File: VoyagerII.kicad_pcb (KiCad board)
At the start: 2 copper layers, 285 x 95.1 mm, 262 parts, among them P1 TC2030-IDC, SW1 SW_PUSH, U1 ATXMEGA32A4U-AU, U2 MCP1700T-3002E/TT, U3 PRTR5V0U2X, U4 IS31FL3731-SALS2, U5 74LVC1G34

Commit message: Adjust line weight for deco
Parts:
- added G***: LOGO, locallib:icon-7.6, F.Cu at (215.5, 133.3)
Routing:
- net COL6: track 144.3 -> 141.3 mm
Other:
- board text added: "CLK"
- board text added: "VCC"
- board text removed: "3.3V"
- board text removed: "PDICLK"

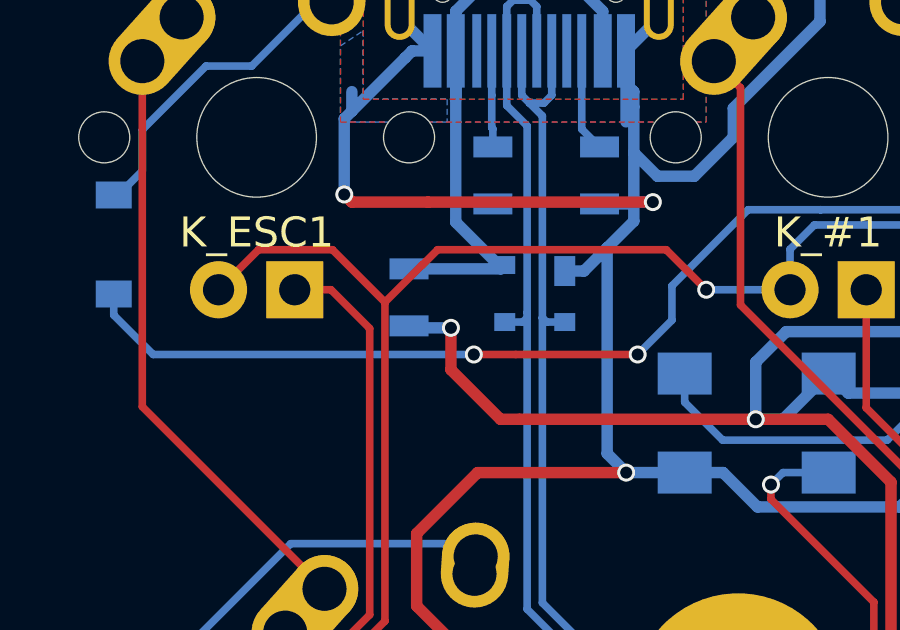
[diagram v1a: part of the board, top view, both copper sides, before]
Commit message: Tune component labels
Horizontal for system, vertical for matrix
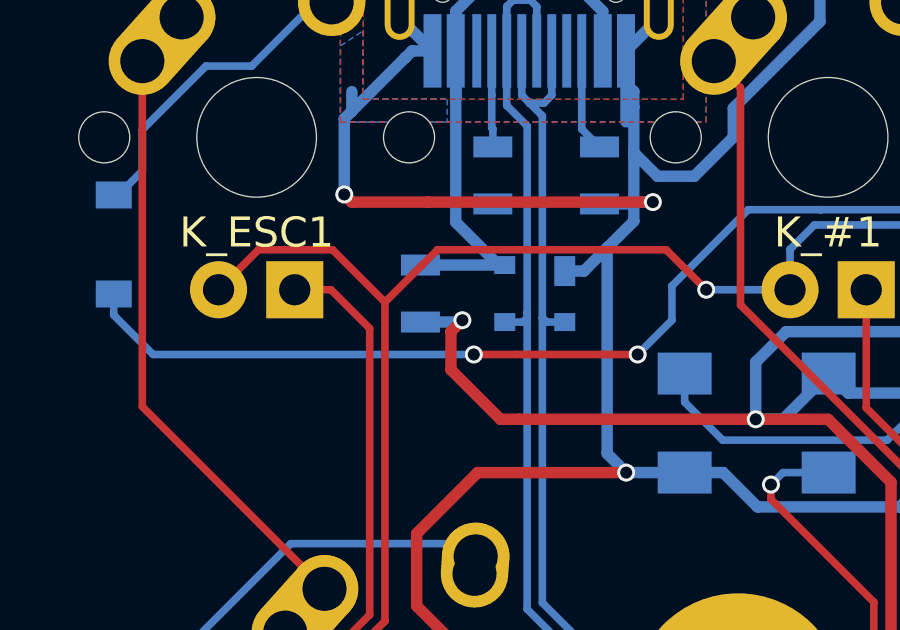
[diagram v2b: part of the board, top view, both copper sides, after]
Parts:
- moved F1 0.40 mm to (62.6, 62.4)
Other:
- board text removed: "Rev. 1.0"
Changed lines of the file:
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@@
     (area 28.932287 28.25625 334.504151 153.909376)
     (thickness 1.6)
-    (drawings 47)
+    (drawings 49)
     (tracks 3211)
     (zones 0)
@@
     (tags "capacitor 0805")
     (attr smd)
-    (fp_text reference C2 (at 0 1.651 270) (layer B.SilkS)
+    (fp_text reference C2 (at -2.54 0 360) (layer B.SilkS)
       (effects (font (size 1 1) (thickness 0.15)) (justify mirror))
     )
@@
     (tags "capacitor 0805")
     (attr smd)
-    (fp_text reference C4 (at 0 1.778 90) (layer B.SilkS)
+    (fp_text reference C4 (at 0 2.032 180) (layer B.SilkS)
       (effects (font (size 1 1) (thickness 0.15)) (justify mirror))
     )
@@
     (tags "resistor 0805")
     (attr smd)
-    (fp_text reference R1 (at 0 -1.778 450) (layer B.SilkS)
+    (fp_text reference R1 (at 0 -2.032 540) (layer B.SilkS)
       (effects (font (size 1 1) (thickness 0.15)) (justify mirror))
     )
@@
     (tags SOD-123)
     (attr smd)
-    (fp_text reference D15 (at 0 2) (layer B.SilkS)
+    (fp_text reference D15 (at -3.175 -0.015875 90) (layer B.SilkS)
       (effects (font (size 1 1) (thickness 0.15)) (justify mirror))
     )
@@
     (tags SOD-123)
     (attr smd)
-    (fp_text reference D29 (at 0 2) (layer B.SilkS)
+    (fp_text reference D29 (at -3.190875 0.015875 90) (layer B.SilkS)
       (effects (font (size 1 1) (thickness 0.15)) (justify mirror))
     )
@@
     (clearance 0.127)
     (attr virtual)
-    (fp_text reference P1 (at -3.048 -2.54 540) (layer B.SilkS)
+    (fp_text reference P1 (at -3.048 2.54 540) (layer B.SilkS)
       (effects (font (size 0.75692 0.75692) (thickness 0.127)) (justify mirror))
     )
@@
     (tags "resistor 0805")
     (attr smd)
-    (fp_text reference R2 (at 0 1.65 270) (layer B.SilkS)
+    (fp_text reference R2 (at 0 2.032 360) (layer B.SilkS)
       (effects (font (size 1 1) (thickness 0.15)) (justify mirror))
     )
@@
     (tags "resistor 0805")
     (attr smd)
-    (fp_text reference R3 (at 0 1.65 90) (layer B.SilkS)
+    (fp_text reference R3 (at -2.413 0 180) (layer B.SilkS)
       (effects (font (size 1 1) (thickness 0.15)) (justify mirror))
     )
@@
     (tags "resistor 0805")
     (attr smd)
-    (fp_text reference R4 (at 0 1.65 90) (layer B.SilkS)
+    (fp_text reference R4 (at -2.413 0 180) (layer B.SilkS)
       (effects (font (size 1 1) (thickness 0.15)) (justify mirror))
     )
@@
     (tags "capacitor 0805")
     (attr smd)
-    (fp_text reference CRGB1 (at 2.54 -1.778 360) (layer B.SilkS)
+    (fp_text reference CRGB1 (at 2.54 -2.032 360) (layer B.SilkS)
       (effects (font (size 1 1) (thickness 0.15)) (justify mirror))
     )
@@
     (tags "resistor 0805")
     (attr smd)
-    (fp_text reference R5 (at 0 1.65 90) (layer B.SilkS)
+    (fp_text reference R5 (at 0 -2.032 180) (layer B.SilkS)
       (effects (font (size 1 1) (thickness 0.15)) (justify mirror))
     )
@@
     (tags "SOT-353 SC-70-5")
     (attr smd)
-    (fp_text reference U5 (at -0.762 -2.159) (layer B.SilkS)
+    (fp_text reference U5 (at -2.54 0) (layer B.SilkS)
       (effects (font (size 1 1) (thickness 0.15)) (justify mirror))
     )
@@
   )
   (module Resistors_SMD:R_0805 (layer B.Cu)
-    (at 62.23 62.484 90)
+    (at 62.611 62.357 90)
     (descr "Resistor SMD 0805, reflow soldering, Vishay (see dcrcw.pdf)")
     (tags "resistor 0805")
     (attr smd)
-    (fp_text reference F1 (at 2.286 -0.0635 180) (layer B.SilkS)
+    (fp_text reference F1 (at -2.413 0 180) (layer B.SilkS)
       (effects (font (size 1 1) (thickness 0.15)) (justify mirror))
     )
@@
   (module locallib:SOT143B (layer B.Cu)
     (at 66.421 62.357 270)
-    (fp_text reference U3 (at -2.286 -0.0635 540) (layer B.SilkS)
+    (fp_text reference U3 (at 2.413 0 540) (layer B.SilkS)
       (effects (font (size 1 1) (thickness 0.15)) (justify mirror))
     )
@@
     (tags SOD-123)
     (attr smd)
-    (fp_text reference D63 (at 0 2 90) (layer B.SilkS)
+    (fp_text reference D63 (at 0.53975 -1.93675 90) (layer B.SilkS)
       (effects (font (size 1 1) (thickness 0.15)) (justify mirror))
     )
@@
     (tags SOD-123)
     (attr smd)
-    (fp_text reference D64 (at 0 2) (layer B.SilkS)
+    (fp_text reference D64 (at -3.20675 -0.015875 90) (layer B.SilkS)
       (effects (font (size 1 1) (thickness 0.15)) (justify mirror))
     )
@@
     (tags "resistor 0805")
     (attr smd)
-    (fp_text reference R6 (at 0.762 1.778 270) (layer B.SilkS)
+    (fp_text reference R6 (at -1.016 -2.032 360) (layer B.SilkS)
       (effects (font (size 1 1) (thickness 0.15)) (justify mirror))
     )
@@
     (tags "resistor 0805")
     (attr smd)
-    (fp_text reference R7 (at 2.413 -0.254 360) (layer B.SilkS)
+    (fp_text reference R7 (at 1.016 -2.032 360) (layer B.SilkS)
       (effects (font (size 1 1) (thickness 0.15)) (justify mirror))
     )
@@
       (xy 1.69672 0.335006) (xy 1.69672 1.69672)) (layer F.Mask) (width 0.01))
   )
+  (gr_line (start 70.739 55.88) (end 70.739 53.467) (layer B.SilkS) (width 0.3))
+  (gr_line (start 61.722 55.88) (end 70.739 55.88) (layer B.SilkS) (width 0.3))
+  (gr_line (start 61.722 53.467) (end 61.722 55.88) (layer B.SilkS) (width 0.3))
   (gr_text "Rev 1.5" (at 66.167 50.419) (layer B.SilkS)
     (effects (font (size 1 1) (thickness 0.15)) (justify mirror))
@@
     (arrow2b (pts (xy 36.068 47.879) (xy 35.481579 46.752496)))
   )
-  (gr_text "Rev. 1.0" (at 145.669 140.335) (layer B.SilkS)
-    (effects (font (size 1 1) (thickness 0.15)) (justify mirror))
-  )
   (gr_line (start 210.058 130.937) (end 210.058 136.017) (layer B.SilkS) (width 0.15))
   (gr_text "Lo and\nBehold!" (at 207.899 133.477 90) (layer B.SilkS)
@@
   (segment (start 136.255 134.618) (end 135.310499 135.562501) (width 0.381) (layer B.Cu) (net 2) (status 10))
   (segment (start 135.310499 135.562501) (end 130.500501 135.562501) (width 0.381) (layer B.Cu) (net 2))
+  (segment (start 64.008 63.246) (end 63.627 63.627) (width 0.381) (layer F.Cu) (net 3))
+  (segment (start 63.627 63.627) (end 63.627 64.897) (width 0.381) (layer F.Cu) (net 3))
+  (segment (start 62.611 63.307) (end 63.947 63.307) (width 0.381) (layer B.Cu) (net 3))
+  (segment (start 63.947 63.307) (end 64.008 63.246) (width 0.381) (layer B.Cu) (net 3))
+  (via (at 64.008 63.246) (size 0.6) (drill 0.4) (layers F.Cu B.Cu) (net 3))
   (segment (start 155.448 65.659) (end 155.448 108.712) (width 0.381) (layer F.Cu) (net 3))
   (segment (start 155.448 108.712) (end 156.337 109.601) (width 0.381) (layer F.Cu) (net 3))
@@
   (segment (start 236.461138 128.003138) (end 236.347 127.889) (width 0.381) (layer B.Cu) (net 3))
   (via (at 236.347 127.889) (size 0.6) (drill 0.4) (layers F.Cu B.Cu) (net 3))
-  (segment (start 63.627 63.5) (end 62.296 63.5) (width 0.381) (layer B.Cu) (net 3))
-  (segment (start 62.296 63.5) (end 62.23 63.434) (width 0.381) (layer B.Cu) (net 3))
   (segment (start 65.278 66.548) (end 63.627 64.897) (width 0.381) (layer F.Cu) (net 3))
-  (segment (start 63.627 64.897) (end 63.627 63.5) (width 0.381) (layer F.Cu) (net 3))
-  (via (at 63.627 63.5) (size 0.6) (drill 0.4) (layers F.Cu B.Cu) (net 3))
   (segment (start 65.913 66.548) (end 65.278 66.548) (width 0.381) (layer F.Cu) (net 3))
   (segment (start 73.787 66.548) (end 76.2 66.548) (width 0.381) (layer F.Cu) (net 3))
@@
   (via (at 132.715 129.413) (size 0.6) (drill 0.4) (layers F.Cu B.Cu) (net 3))
   (via (at 153.83404 137.460048) (size 0.6) (drill 0.4) (layers F.Cu B.Cu) (net 3))
+  (segment (start 62.611 61.407) (end 65.421 61.407) (width 0.381) (layer B.Cu) (net 4))
   (segment (start 65.217 61.407) (end 65.421 61.407) (width 0.381) (layer B.Cu) (net 4))
   (segment (start 63.7876 59.9776) (end 65.217 61.407) (width 0.381) (layer B.Cu) (net 4))
@@
   (segment (start 67.746412 52.00649) (end 68.6876 52.947678) (width 0.381) (layer B.Cu) (net 4))
   (segment (start 68.6876 52.947678) (end 68.6876 54.269) (width 0.381) (layer B.Cu) (net 4))
-  (segment (start 62.23 61.534) (end 65.294 61.534) (width 0.381) (layer B.Cu) (net 4))
-  (segment (start 65.294 61.534) (end 65.421 61.407) (width 0.381) (layer B.Cu) (net 4))
   (segment (start 155.067 129.032) (end 154.813 128.778) (width 0.254) (layer F.Cu) (net 5))
   (segment (start 164.592 138.049) (end 163.957 137.414) (width 0.254) (layer F.Cu) (net 5) (status 10))

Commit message: Update readme
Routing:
- net GND: track 1577.1 -> 1592.0 mm, vias 72 -> 74
- net LED-A4: track 224.5 -> 223.7 mm

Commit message: Add logo
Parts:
- added G***: LOGO, locallib:ai-7.6, F.Cu at (227.4, 133.3)
- added REF**: ai03-20mil, locallib:ai03-20mil, B.Cu at (73.8, 133.2)
- moved G*** 0.65 mm to (216.2, 133.3)

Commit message: Finalize PCB, DRC checks
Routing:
- net GND: track 1592.0 -> 1590.9 mm
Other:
- net class Default: clearance 0.2032 -> 0.1778
- net class Power: clearance 0.2032 -> 0.1778
- rule trace_clearance: 0.2032 -> 0.1778
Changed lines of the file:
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@@
 (kicad_pcb (version 4) (host pcbnew 4.0.7)
   (general
-    (links 0)
-    (no_connects 1)
+    (links 646)
+    (no_connects 0)
     (area 28.932287 28.25625 334.504151 153.909376)
     (thickness 1.6)
     (drawings 43)
-    (tracks 3236)
+    (tracks 3224)
     (zones 0)
     (modules 265)
@@
   (setup
     (last_trace_width 0.254)
-    (trace_clearance 0.2032)
+    (trace_clearance 0.1778)
     (zone_clearance 0.381)
     (zone_45_only no)
@@
   (net 143 "Net-(USB1-Pad3)")
   (net_class Default "This is the default net class."
-    (clearance 0.2032)
+    (clearance 0.1778)
     (trace_width 0.254)
     (via_dia 0.6)
@@
   )
   (net_class Power ""
-    (clearance 0.2032)
+    (clearance 0.1778)
     (trace_width 0.381)
     (via_dia 0.6)
@@
   (segment (start 153.807 132.318) (end 153.188 131.699) (width 0.381) (layer B.Cu) (net 1))
   (segment (start 153.188 131.699) (end 151.1785 131.699) (width 0.381) (layer B.Cu) (net 1) (status 20))
-  (segment (start 66.167 48.674) (end 61.9176 48.674) (width 0.381) (layer B.Cu) (net 2))
-  (segment (start 70.5576 48.674) (end 66.167 48.674) (width 0.381) (layer B.Cu) (net 2))
+  (segment (start 69.85 50.9905) (end 67.5335 48.674) (width 0.381) (layer B.Cu) (net 2))
+  (segment (start 67.5335 48.674) (end 66.167 48.674) (width 0.381) (layer B.Cu) (net 2))
+  (segment (start 69.85 52.627686) (end 69.85 50.9905) (width 0.381) (layer B.Cu) (net 2))
+  (segment (start 69.4626 54.269) (end 69.4626 53.015086) (width 0.381) (layer B.Cu) (net 2))
+  (segment (start 69.4626 53.015086) (end 69.85 52.627686) (width 0.381) (layer B.Cu) (net 2))
+  (segment (start 70.5576 48.674) (end 70.5576 52.854) (width 0.381) (layer F.Cu) (net 2))
+  (segment (start 66.167 48.674) (end 66.591264 48.674) (width 0.381) (layer F.Cu) (net 2))
+  (segment (start 66.591264 48.674) (end 70.5576 48.674) (width 0.381) (layer F.Cu) (net 2))
+  (segment (start 61.9176 48.674) (end 61.9176 52.854) (width 0.381) (layer F.Cu) (net 2))
+  (segment (start 66.167 48.674) (end 65.742736 48.674) (width 0.381) (layer F.Cu) (net 2))
+  (segment (start 65.742736 48.674) (end 61.9176 48.674) (width 0.381) (layer F.Cu) (net 2))
+  (segment (start 63.0126 54.269) (end 63.0126 53.015086) (width 0.381) (layer B.Cu) (net 2))
+  (segment (start 63.0126 53.015086) (end 62.611 52.613486) (width 0.381) (layer B.Cu) (net 2))
+  (segment (start 62.611 52.613486) (end 62.611 51.2445) (width 0.381) (layer B.Cu) (net 2))
+  (segment (start 62.611 51.2445) (end 65.1815 48.674) (width 0.381) (layer B.Cu) (net 2))
+  (segment (start 65.1815 48.674) (end 66.167 48.674) (width 0.381) (layer B.Cu) (net 2))
   (via (at 66.167 48.674) (size 0.6) (drill 0.4) (layers F.Cu B.Cu) (net 2))
-  (segment (start 70.5576 53.174) (end 69.7566 53.975) (width 0.381) (layer B.Cu) (net 2))
-  (segment (start 69.7566 53.975) (end 69.4626 54.269) (width 0.381) (layer B.Cu) (net 2))
-  (segment (start 69.85 53.467) (end 69.85 53.8816) (width 0.381) (layer B.Cu) (net 2))
-  (segment (start 69.85 53.8816) (end 69.7566 53.975) (width 0.381) (layer B.Cu) (net 2))
-  (segment (start 70.5576 52.854) (end 70.5576 53.174) (width 0.381) (layer B.Cu) (net 2))
-  (segment (start 62.2351 53.0911) (end 62.738 53.594) (width 0.381) (layer B.Cu) (net 2))
-  (segment (start 62.2351 51.181) (end 61.9176 50.8635) (width 0.381) (layer B.Cu) (net 2))
-  (segment (start 62.5475 51.4934) (end 62.2351 51.181) (width 0.381) (layer B.Cu) (net 2))
-  (segment (start 62.2351 51.181) (end 62.2351 53.0911) (width 0.381) (layer B.Cu) (net 2))
-  (segment (start 70.231 53.086) (end 69.85 53.467) (width 0.381) (layer B.Cu) (net 2))
-  (segment (start 70.231 51.1901) (end 70.5576 50.8635) (width 0.381) (layer B.Cu) (net 2))
-  (segment (start 69.977 51.4441) (end 70.231 51.1901) (width 0.381) (layer B.Cu) (net 2))
-  (segment (start 70.231 51.1901) (end 70.231 53.086) (width 0.381) (layer B.Cu) (net 2))
-  (segment (start 70.5576 48.674) (end 70.5576 50.8635) (width 0.381) (layer B.Cu) (net 2))
-  (segment (start 70.5576 50.8635) (end 70.5576 52.854) (width 0.381) (layer B.Cu) (net 2))
-  (segment (start 69.977 52.8296) (end 69.977 51.4441) (width 0.381) (layer B.Cu) (net 2))
-  (segment (start 69.4626 54.269) (end 69.4626 53.344) (width 0.381) (layer B.Cu) (net 2))
-  (segment (start 69.4626 53.344) (end 69.977 52.8296) (width 0.381) (layer B.Cu) (net 2))
-  (segment (start 61.9176 49.855) (end 61.9176 50.8635) (width 0.381) (layer B.Cu) (net 2))
-  (segment (start 61.9176 50.8635) (end 61.9176 52.854) (width 0.381) (layer B.Cu) (net 2))
-  (segment (start 62.5475 52.8789) (end 62.5475 51.4934) (width 0.381) (layer B.Cu) (net 2))
-  (segment (start 63.0126 54.269) (end 63.0126 53.344) (width 0.381) (layer B.Cu) (net 2))
-  (segment (start 63.0126 53.344) (end 62.5475 52.8789) (width 0.381) (layer B.Cu) (net 2))
   (segment (start 62.865 59.309) (end 65.024 59.309) (width 0.381) (layer F.Cu) (net 2))
   (segment (start 65.024 59.309) (end 70.358 59.309) (width 0.381) (layer F.Cu) (net 2))
@@
   (segment (start 69.662 59.37) (end 69.723 59.309) (width 0.381) (layer B.Cu) (net 2))
   (segment (start 68.06 61.607) (end 67.421 61.607) (width 0.381) (layer B.Cu) (net 2))
-  (segment (start 61.9176 52.854) (end 61.9176 53.174) (width 0.381) (layer B.Cu) (net 2))
-  (segment (start 61.9176 53.174) (end 63.0126 54.269) (width 0.381) (layer B.Cu) (net 2))
-  (segment (start 61.9176 48.674) (end 61.9176 49.855) (width 0.381) (layer B.Cu) (net 2))
   (segment (start 288.544 119.432834) (end 294.104567 124.993401) (width 0.381) (layer F.Cu) (net 2))
   (segment (start 294.104567 124.993401) (end 300.413335 124.993401) (width 0.381) (layer F.Cu) (net 2))
@@
   (segment (start 178.893038 79.121) (end 179.705 79.932962) (width 0.254) (layer B.Cu) (net 112))
   (segment (start 179.705 79.932962) (end 179.705 81.28) (width 0.254) (layer B.Cu) (net 112) (status 20))
+  (segment (start 89.2175 100.33) (end 88.265001 99.377501) (width 0.254) (layer F.Cu) (net 113))
+  (segment (start 79.375 90.9955) (end 79.375 68.072) (width 0.254) (layer F.Cu) (net 113))
+  (segment (start 79.375 68.072) (end 77.47 66.167) (width 0.254) (layer F.Cu) (net 113))
+  (segment (start 88.265001 99.377501) (end 86.169501 99.377501) (width 0.254) (layer F.Cu) (net 113))
+  (segment (start 82.513882 95.721882) (end 82.513882 94.134382) (width 0.254) (layer F.Cu) (net 113))
+  (segment (start 86.169501 99.377501) (end 82.513882 95.721882) (width 0.254) (layer F.Cu) (net 113))
+  (segment (start 82.513882 94.134382) (end 79.375 90.9955) (width 0.254) (layer F.Cu) (net 113))
+  (segment (start 77.47 66.167) (end 77.47 62.23) (width 0.254) (layer F.Cu) (net 113))
   (segment (start 89.2175 100.33) (end 92.329 103.4415) (width 0.254) (layer F.Cu) (net 113))
   (segment (start 92.329 103.4415) (end 92.329 123.825) (width 0.254) (layer F.Cu) (net 113))
@@
   (segment (start 63.02375 98.982962) (end 63.02375 100.33) (width 0.254) (layer B.Cu) (net 113))
   (segment (start 110.8075 138.43) (end 113.03 138.43) (width 0.254) (layer F.Cu) (net 113))
-  (segment (start 89.2175 100.33) (end 88.265001 99.377501) (width 0.254) (layer F.Cu) (net 113) (status 10))
-  (segment (start 88.265001 99.377501) (end 86.169501 99.377501) (width 0.254) (layer F.Cu) (net 113))
-  (segment (start 86.169501 99.377501) (end 82.513882 95.721882) (width 0.254) (layer F.Cu) (net 113))
-  (segment (start 82.513882 94.488) (end 79.375 91.349118) (width 0.254) (layer F.Cu) (net 113))
-  (segment (start 82.513882 95.721882) (end 82.513882 94.488) (width 0.254) (layer F.Cu) (net 113))
-  (segment (start 79.375 91.349118) (end 79.375 68.072) (width 0.254) (layer F.Cu) (net 113))
-  (segment (start 79.375 68.072) (end 77.47 66.167) (width 0.254) (layer F.Cu) (net 113))
-  (segment (start 77.47 66.167) (end 77.47 62.23) (width 0.254) (layer F.Cu) (net 113) (status 20))
   (segment (start 205.815802 132.375) (end 205.936001 132.254801) (width 0.254) (layer B.Cu) (net 113))
   (segment (start 205.936001 132.254801) (end 205.936001 128.595199) (width 0.254) (layer B.Cu) (net 113))
